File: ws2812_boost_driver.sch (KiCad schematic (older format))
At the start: 21 parts, among them J1 Conn_01x01, J2 Conn_01x01, J3 Conn_01x01, J4 Conn_01x01, J5 Conn_01x01, J6 Conn_01x01, J7 Conn_01x01, J8 Conn_ARM_JTAG_SWD_10, U1 ATSAMD21E15L-A, U2 TC2014-3.3VxCTTR, U3 MCP1640CH

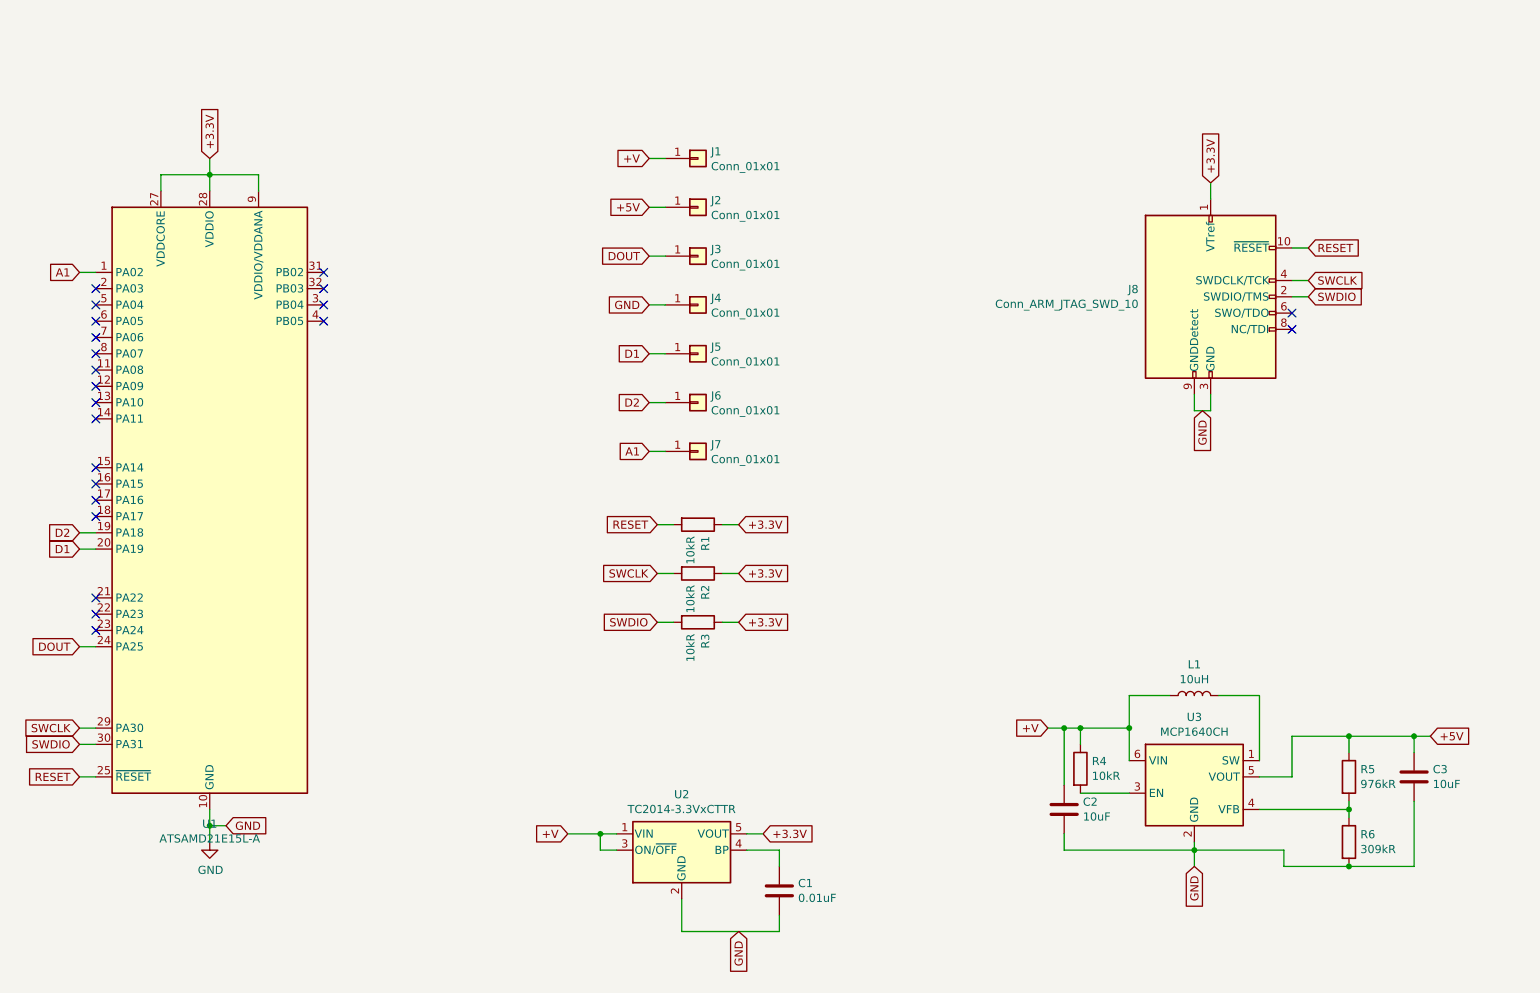
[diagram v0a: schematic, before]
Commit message: Add attiny10 hardware spi->ws2812 support
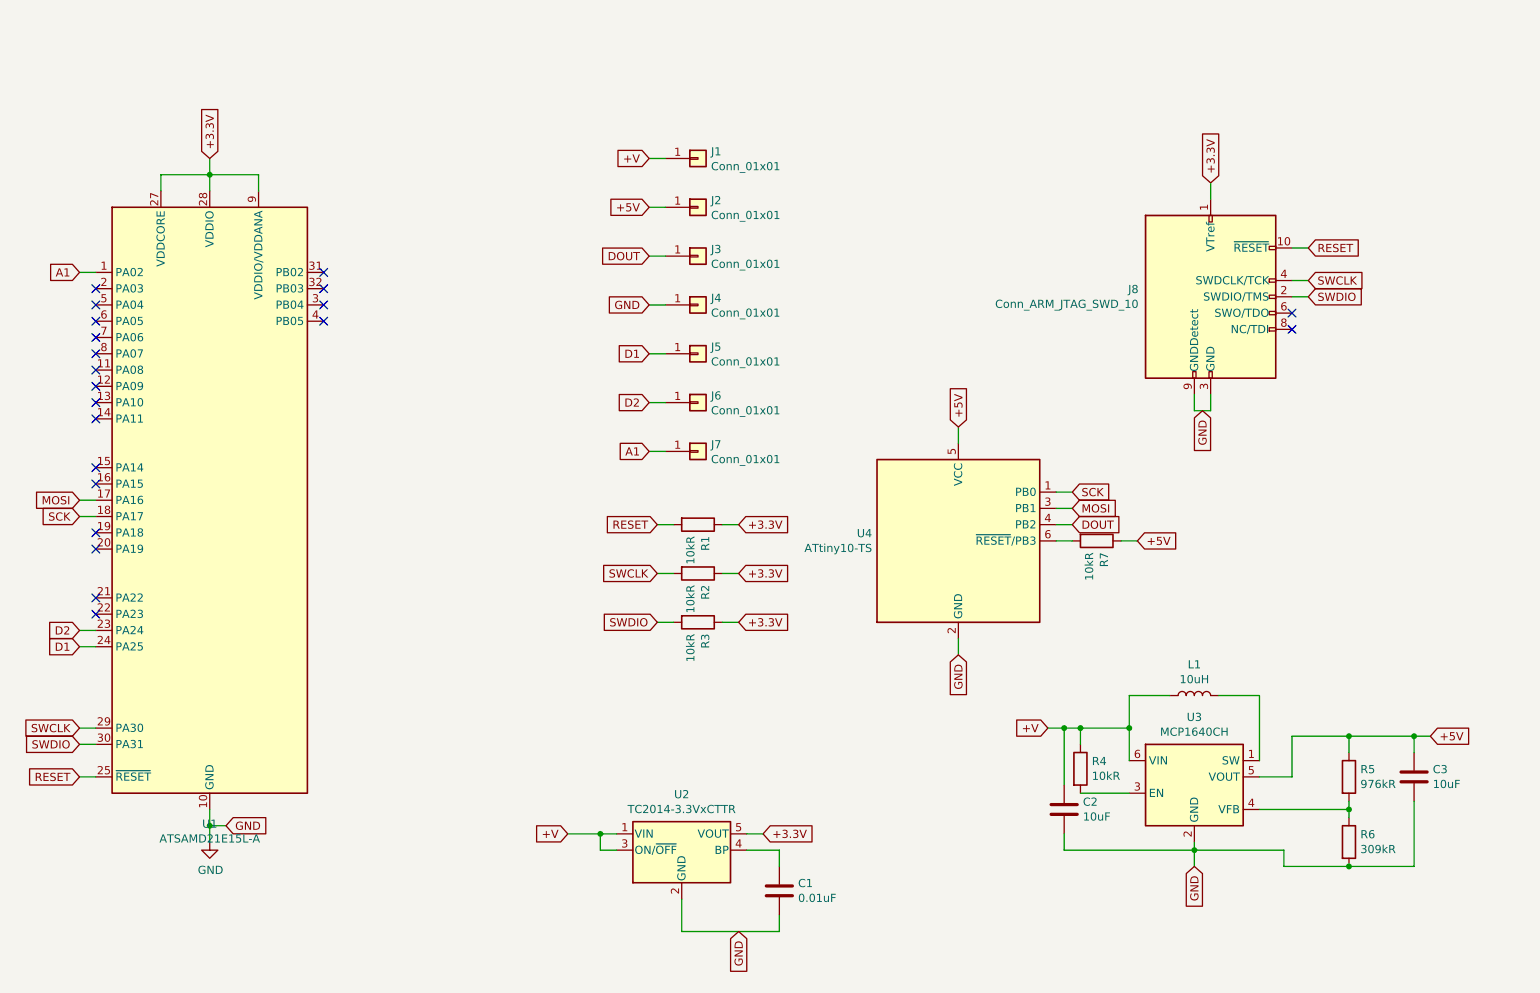
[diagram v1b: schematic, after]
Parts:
- added R7: 10kR, Resistor_SMD:R_0805_2012Metric, symbol Device:R
- added U4: ATtiny10-TS, Package_TO_SOT_SMD:SOT-23-6, symbol MCU_Microchip_ATtiny:ATtiny10-TS
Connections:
- net +5V: now also R7.1, U4.5 (VCC)
- net D1: now also U1.24 (PA25); no longer U1.20 (PA19)
- net D2: now also U1.23 (PA24); no longer U1.19 (PA18)
- net DOUT: now also U4.4 (PB2); no longer U1.24 (PA25)
- net GND: now also U4.2 (GND)
- net MOSI: now reaches U1.17 (PA16)
- net MOSI: now also U4.3 (PB1)
- net SCK: now reaches U1.18 (PA17)
- net SCK: now also U4.1 (PB0)
- new net: R7.2, U4.6 (~RESET~/PB3)
- no-connect marks 22 -> 21
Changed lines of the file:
@@
 Text GLabel 5600 3200 0    50   Input ~ 0
 A1
+Text GLabel 8200 3650 2    50   Input ~ 0
+DOUT
+Wire Wire Line
+	8200 3650 8100 3650
 Text GLabel 2100 4400 0    50   Input ~ 0
-DOUT
-Wire Wire Line
-	2100 4400 2200 4400
-Text GLabel 2100 3800 0    50   Input ~ 0
 D1
-Text GLabel 2100 3700 0    50   Input ~ 0
+Text GLabel 2100 4300 0    50   Input ~ 0
 D2
 Text GLabel 2100 2100 0    50   Input ~ 0
@@
 	2200 2100 2100 2100
 Wire Wire Line
-	2200 3700 2100 3700
-Wire Wire Line
-	2100 3800 2200 3800
+	2200 4300 2100 4300
+Wire Wire Line
+	2100 4400 2200 4400
 NoConn ~ 3600 2100
 NoConn ~ 3600 2200
@@
 NoConn ~ 2200 3300
 NoConn ~ 2200 3400
-NoConn ~ 2200 3500
-NoConn ~ 2200 3600
+NoConn ~ 2200 3800
+NoConn ~ 2200 3700
 NoConn ~ 2200 4100
 NoConn ~ 2200 4200
-NoConn ~ 2200 4300
 $Comp
 L Regulator_Switching:MCP1640CH U3
@@
 Wire Wire Line
 	5600 1400 5700 1400
+$Comp
+L MCU_Microchip_ATtiny:ATtiny10-TS U4
+U 1 1 5FB0901B
+P 7500 3750
+F 0 "U4" H 6970 3796 50  0000 R CNN
+F 1 "ATtiny10-TS" H 6970 3705 50  0000 R CNN
+F 2 "Package_TO_SOT_SMD:SOT-23-6" H 7500 3750 50  0001 C CIN
+F 3 "http://ww1.microchip.com/downloads/en/DeviceDoc/Atmel-8127-AVR-8-bit-Microcontroller-ATtiny4-ATtiny5-ATtiny9-ATtiny10_Datasheet.pdf" H 7500 3750 50  0001 C CNN
+	1    7500 3750
+	1    0    0    -1
+$EndComp
+Text GLabel 7500 3050 1    50   Input ~ 0
++5V
+Wire Wire Line
+	7500 3050 7500 3150
+Text GLabel 7500 4450 3    50   Input ~ 0
+GND
+Wire Wire Line
+	7500 4450 7500 4350
+Wire Wire Line
+	8200 3750 8100 3750
+Wire Wire Line
+	8600 3750 8500 3750
+Text GLabel 8600 3750 2    50   Input ~ 0
++5V
+$Comp
+L Device:R R7
+U 1 1 5FB0D6BE
+P 8350 3750
+F 0 "R7" H 8420 3796 50  0000 L CNN
+F 1 "10kR" H 8420 3705 50  0000 L CNN
+F 2 "Resistor_SMD:R_0805_2012Metric" V 8280 3750 50  0001 C CNN
+F 3 "~" H 8350 3750 50  0001 C CNN
+	1    8350 3750
+	0    1    1    0
+$EndComp
+Text GLabel 2100 3600 0    50   Input ~ 0
+SCK
+Text GLabel 2100 3500 0    50   Input ~ 0
+MOSI
+Wire Wire Line
+	2200 3500 2100 3500
+Wire Wire Line
+	2100 3600 2200 3600
+Text GLabel 8200 3450 2    50   Input ~ 0
+SCK
+Text GLabel 8200 3550 2    50   Input ~ 0
+MOSI
+Wire Wire Line
+	8100 3550 8200 3550
+Wire Wire Line
+	8200 3450 8100 3450
 $EndSCHEMATC

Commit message: Fix core vreg issue
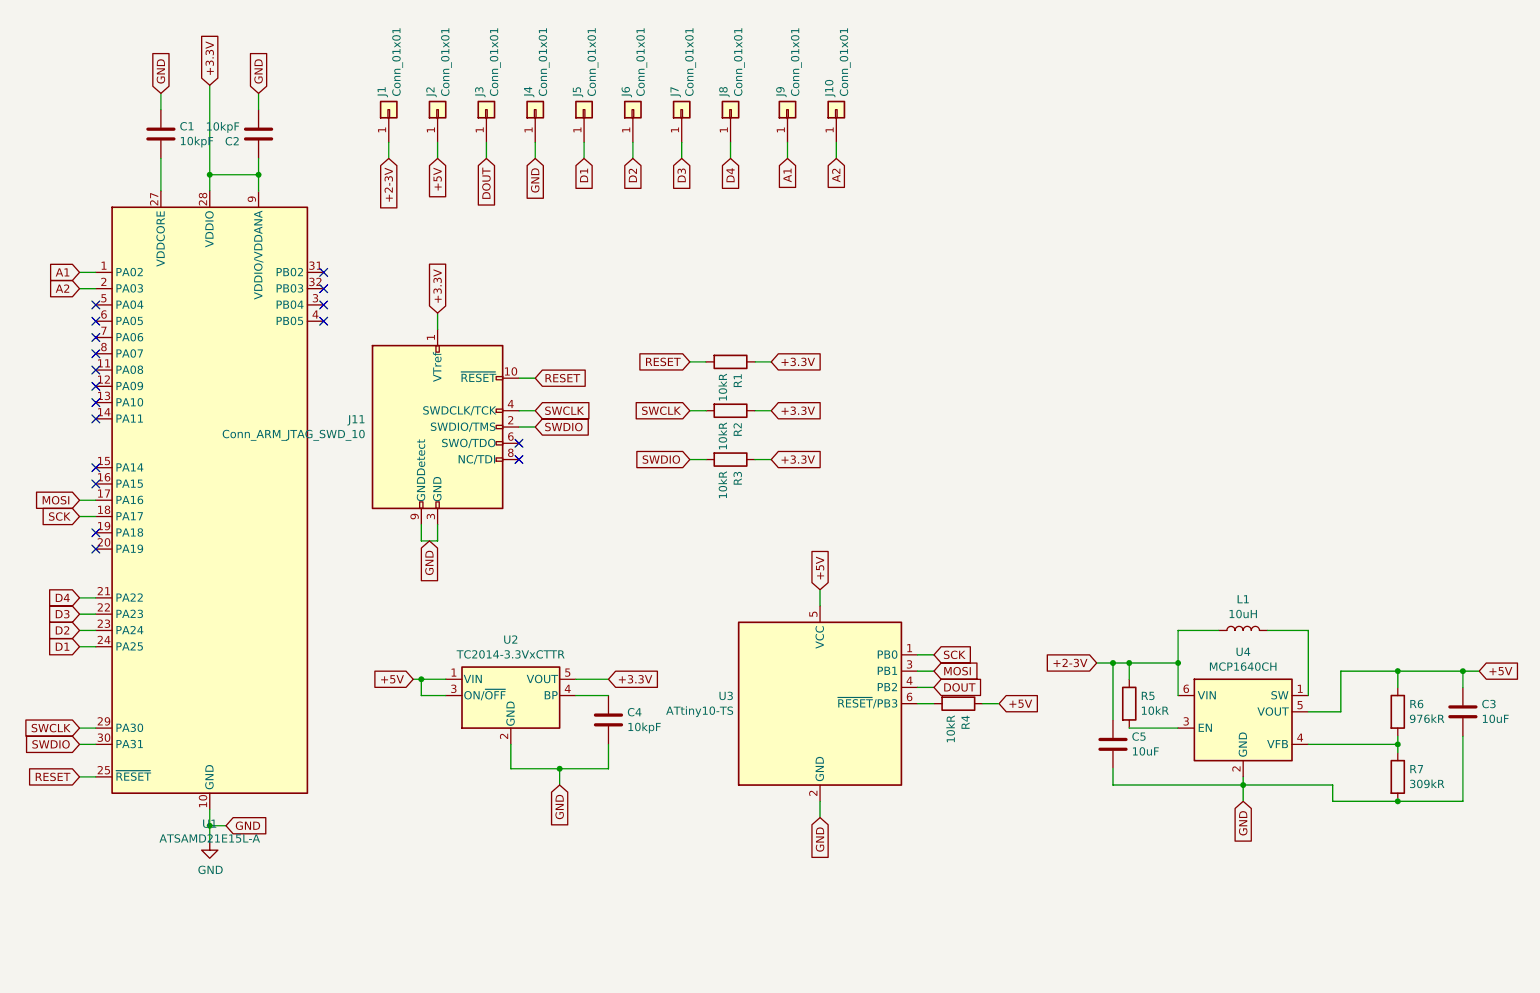
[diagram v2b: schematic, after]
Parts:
- added C2, C4: 10kpF, Capacitor_SMD:C_0603_1608Metric, symbol Device:C
- added J10, J7, J8: Conn_01x01, TestPoint:TestPoint_Pad_1.5x1.5mm, symbol Connector_Generic:Conn_01x01
- C1: value 0.01uF -> 10kpF
- C3: footprint Capacitor_SMD:C_0603_1608Metric -> Capacitor_SMD:C_0805_2012Metric
- C5: renamed from C2; footprint Capacitor_SMD:C_0603_1608Metric -> Capacitor_SMD:C_0805_2012Metric
- J11: renamed from J8; footprint Connector_PinHeader_1.00mm:PinHeader_2x05_P1.00mm_Vertical -> Connector_PinHeader_1.27mm:PinHeader_2x05_P1.27mm_Vertical
- renumbered J7 to J9, R7 to R4, R4 to R5, R5 to R6, R6 to R7, U4 to U3, U3 to U4
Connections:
- net +3.3V: now also C2.1; no longer U1.27 (VDDCORE)
- net +5V: now also U2.1 (VIN), U2.3 (ON/~OFF~)
- net GND: now also C1.1, C2.2, C4.2; no longer C1.2
- net A2: now reaches U1.2 (PA03)
- net A2: now also J10.1 (Pin_1)
- net D4: now reaches U1.21 (PA22)
- net D4: now also J8.1 (Pin_1)
- net D3: now reaches U1.22 (PA23)
- net D3: now also J7.1 (Pin_1)
- net at U2.4 (BP): now also C4.1; no longer C1.1
- net +V renamed +2-3V
- net +2-3V: no longer U2.1 (VIN), U2.3 (ON/~OFF~)
- new net: C1.2, U1.27 (VDDCORE)
- no-connect marks 21 -> 18
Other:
- moved on the sheet: C3, C5, J1, J11, J2, J3, J4, J5, J6, J9, L1, R1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
